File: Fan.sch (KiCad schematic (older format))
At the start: 9 parts

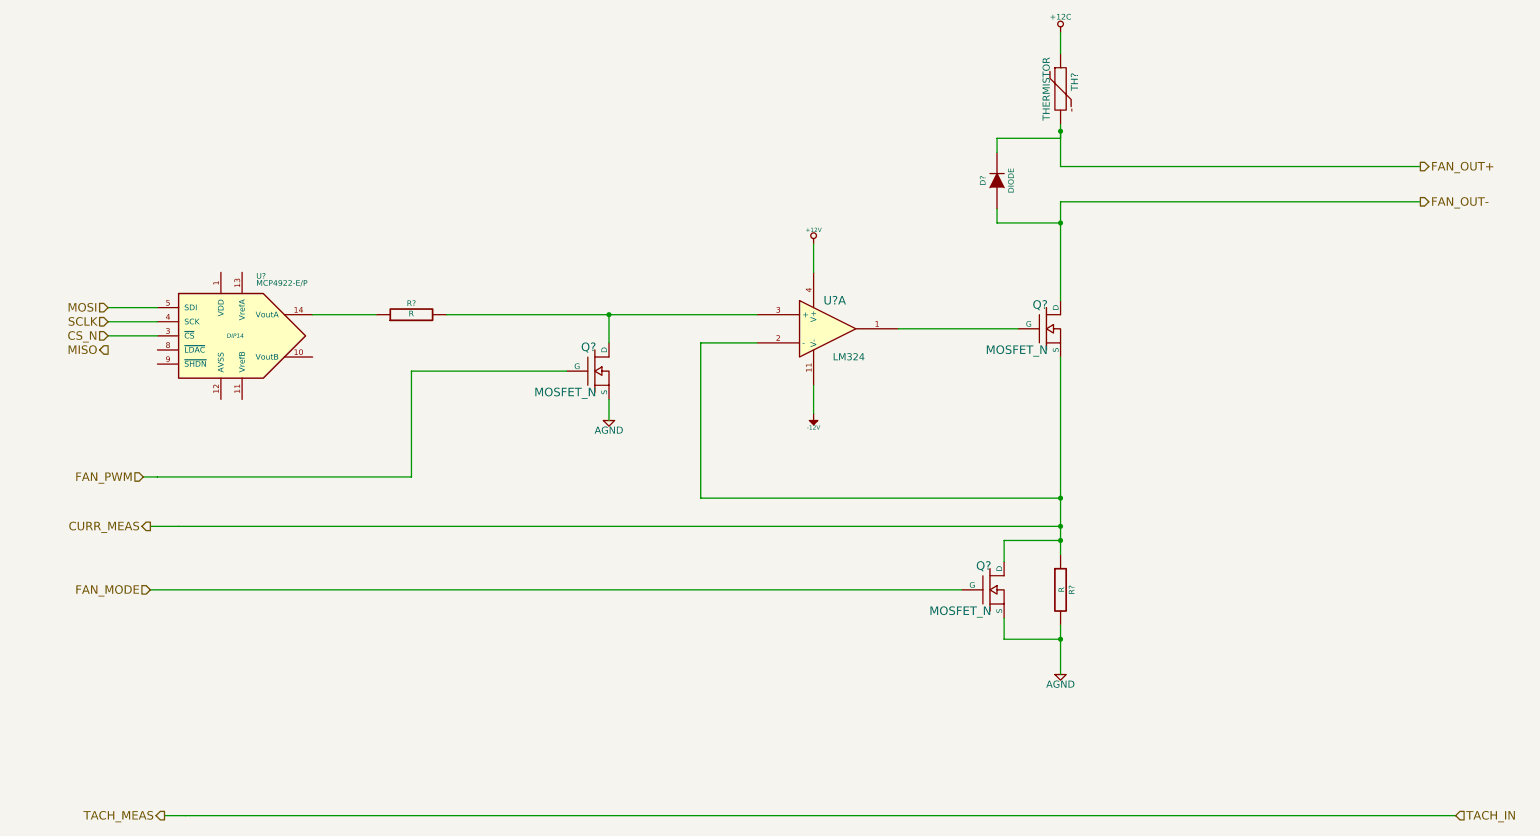
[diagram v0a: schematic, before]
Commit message: Created Footprints and Placed Relay Module
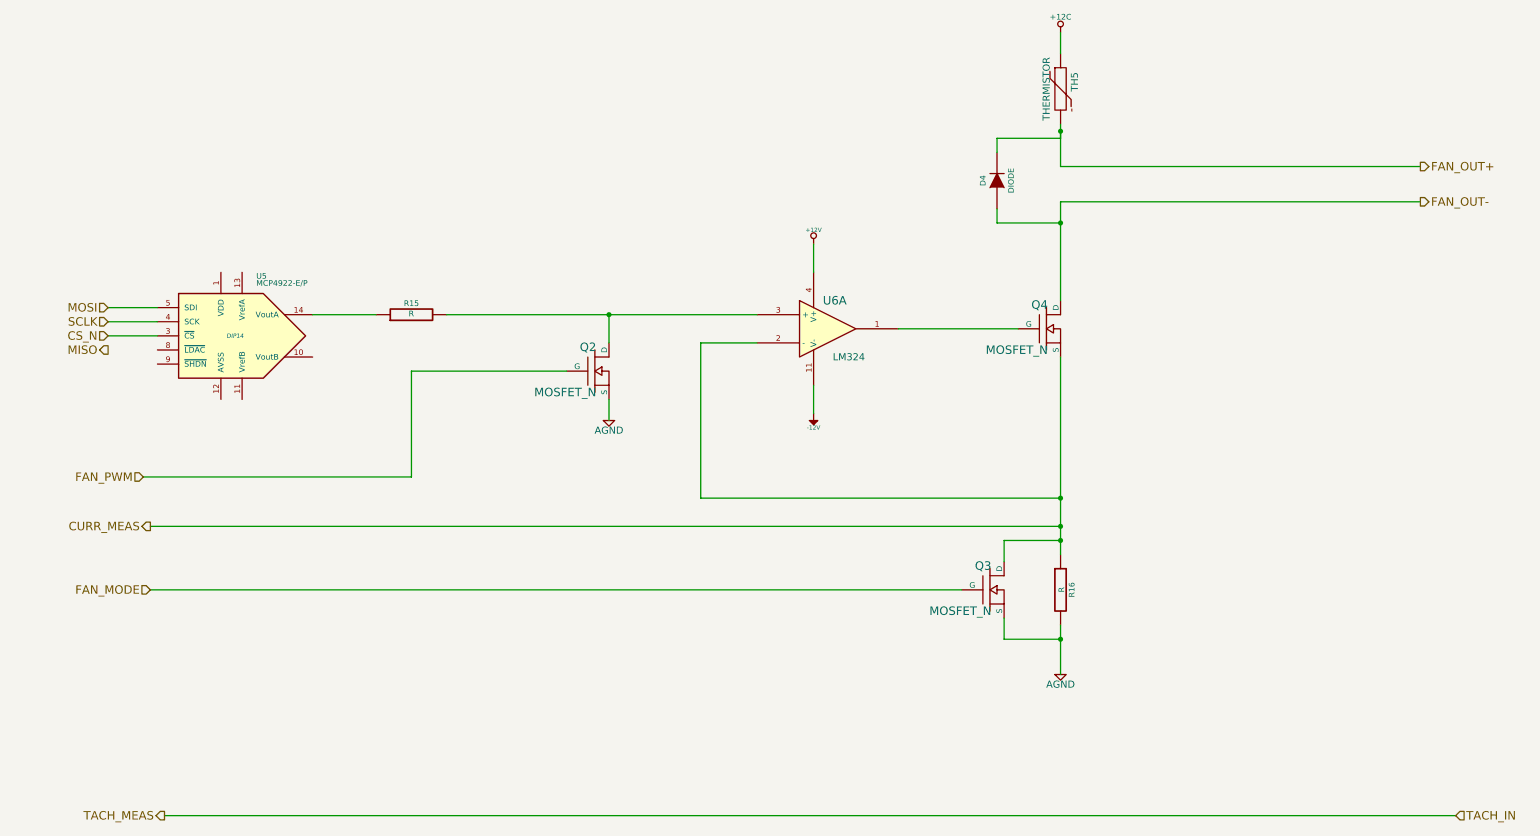
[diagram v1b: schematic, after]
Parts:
- gave numbers to parts that had none: 9
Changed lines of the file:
@@
-EESchema Schematic File Version 2  date 10/10/2013 12:18:22 AM
+EESchema Schematic File Version 2  date 10/10/2013 1:06:29 AM
 LIBS:power
 LIBS:device
@@
 FAN_PWM
 $Comp
-L LM324 U?
+L LM324 U6
 U 1 1 52369784
 P 6250 3100
-F 0 "U?" H 6300 3300 60  0000 C CNN
+F 0 "U6" H 6300 3300 60  0000 C CNN
 F 1 "LM324" H 6400 2900 50  0000 C CNN
 F 2 "" H 6250 3100 60  0000 C CNN
@@
 $EndComp
 $Comp
-L MOSFET_N Q?
+L MOSFET_N Q4
 U 1 1 523697B6
 P 7800 3100
-F 0 "Q?" H 7810 3270 60  0000 R CNN
+F 0 "Q4" H 7810 3270 60  0000 R CNN
 F 1 "MOSFET_N" H 7810 2950 60  0000 R CNN
 F 2 "~" H 7800 3100 60  0000 C CNN
@@
 $EndComp
 $Comp
-L R R?
+L R R16
 U 1 1 523697E7
 P 7900 4950
-F 0 "R?" V 7980 4950 40  0000 C CNN
+F 0 "R16" V 7980 4950 40  0000 C CNN
 F 1 "R" V 7907 4951 40  0000 C CNN
 F 2 "~" V 7830 4950 30  0000 C CNN
@@
 $EndComp
 $Comp
-L AGND #PWR?
+L AGND #PWR31
 U 1 1 523697F6
 P 7900 5550
-F 0 "#PWR?" H 7900 5550 40  0001 C CNN
+F 0 "#PWR31" H 7900 5550 40  0001 C CNN
 F 1 "AGND" H 7900 5480 50  0000 C CNN
 F 2 "" H 7900 5550 60  0000 C CNN
@@
 $EndComp
 $Comp
-L +12V #PWR?
+L +12V #PWR28
 U 1 1 5236981B
 P 6150 2500
-F 0 "#PWR?" H 6150 2450 20  0001 C CNN
+F 0 "#PWR28" H 6150 2450 20  0001 C CNN
 F 1 "+12V" H 6150 2600 30  0000 C CNN
 F 2 "" H 6150 2500 60  0000 C CNN
@@
 $EndComp
 $Comp
-L -12V #PWR?
+L -12V #PWR29
 U 1 1 5236982E
 P 6150 3700
-F 0 "#PWR?" H 6150 3830 20  0001 C CNN
+F 0 "#PWR29" H 6150 3830 20  0001 C CNN
 F 1 "-12V" H 6150 3800 30  0000 C CNN
 F 2 "" H 6150 3700 60  0000 C CNN
@@
 $EndComp
 $Comp
-L AGND #PWR?
+L AGND #PWR27
 U 1 1 523698EE
 P 4700 3750
-F 0 "#PWR?" H 4700 3750 40  0001 C CNN
+F 0 "#PWR27" H 4700 3750 40  0001 C CNN
 F 1 "AGND" H 4700 3680 50  0000 C CNN
 F 2 "" H 4700 3750 60  0000 C CNN
@@
 $EndComp
 $Comp
-L MCP4922-E/P U?
+L MCP4922-E/P U5
 U 1 1 52369914
 P 2050 3150
-F 0 "U?" H 2200 3550 40  0000 L BNN
+F 0 "U5" H 2200 3550 40  0000 L BNN
 F 1 "MCP4922-E/P" H 2200 3500 40  0000 L BNN
 F 2 "DIP14" H 2050 3150 30  0000 C CIN
@@
 CURR_MEAS
 $Comp
-L R R?
+L R R15
 U 1 1 52369992
 P 3300 3000
-F 0 "R?" V 3380 3000 40  0000 C CNN
+F 0 "R15" V 3380 3000 40  0000 C CNN
 F 1 "R" V 3307 3001 40  0000 C CNN
 F 2 "~" V 3230 3000 30  0000 C CNN
@@
 SCLK
 $Comp
-L MOSFET_N Q?
+L MOSFET_N Q3
 U 1 1 5243896F
 P 7400 4950
-F 0 "Q?" H 7410 5120 60  0000 R CNN
+F 0 "Q3" H 7410 5120 60  0000 R CNN
 F 1 "MOSFET_N" H 7410 4800 60  0000 R CNN
 F 2 "~" H 7400 4950 60  0000 C CNN
@@
 $EndComp
 $Comp
-L THERMISTOR TH?
+L THERMISTOR TH5
 U 1 1 5243899F
 P 7900 1400
-F 0 "TH?" V 8000 1450 50  0000 C CNN
+F 0 "TH5" V 8000 1450 50  0000 C CNN
 F 1 "THERMISTOR" V 7800 1400 50  0000 C CNN
 F 2 "~" H 7900 1400 60  0000 C CNN
@@
 $EndComp
 $Comp
-L DIODE D?
+L DIODE D4
 U 1 1 52438A1C
 P 7450 2050
-F 0 "D?" H 7450 2150 40  0000 C CNN
+F 0 "D4" H 7450 2150 40  0000 C CNN
 F 1 "DIODE" H 7450 1950 40  0000 C CNN
 F 2 "~" H 7450 2050 60  0000 C CNN
@@
 $EndComp
 $Comp
-L MOSFET_N Q?
+L MOSFET_N Q2
 U 1 1 52438CB2
 P 4600 3400
-F 0 "Q?" H 4610 3570 60  0000 R CNN
+F 0 "Q2" H 4610 3570 60  0000 R CNN
 F 1 "MOSFET_N" H 4610 3250 60  0000 R CNN
 F 2 "~" H 4600 3400 60  0000 C CNN
@@
 	7600 3100 6750 3100
 Wire Wire Line
-	7900 3300 7900 4300
-Wire Wire Line
-	7900 4300 7900 4500
-Wire Wire Line
-	7900 4500 7900 4600
-Wire Wire Line
-	7900 4600 7900 4700
-Wire Wire Line
-	7900 5200 7900 5300
-Wire Wire Line
-	7900 5300 7900 5550
+	7900 3300 7900 4700
+Wire Wire Line
+	7900 5200 7900 5550
 Wire Wire Line
 	5350 4300 5350 3200
@@
 	6150 3700 6150 3500
 Wire Wire Line
-	3550 3000 4700 3000
-Wire Wire Line
-	4700 3000 5750 3000
+	3550 3000 5750 3000
 Wire Wire Line
 	4700 3600 4700 3750
 Wire Wire Line
-	7900 4500 1650 4500
-Wire Wire Line
-	1650 4500 1450 4500
+	1450 4500 7900 4500
 Connection ~ 7900 4500
 Wire Wire Line
-	1400 4150 1500 4150
-Wire Wire Line
-	1500 4150 3300 4150
+	1400 4150 3300 4150
 Wire Wire Line
 	2600 3000 3050 3000
@@
 	7900 1000 7900 1150
 Wire Wire Line
-	7900 1650 7900 1700
-Wire Wire Line
-	7900 1700 7900 1950
+	7900 1650 7900 1950
 Wire Wire Line
 	7900 1950 10450 1950
@@
 	10450 2200 7900 2200
 Wire Wire Line
-	7900 2200 7900 2350
-Wire Wire Line
-	7900 2350 7900 2900
+	7900 2200 7900 2900
 Wire Wire Line
 	7900 2350 7450 2350
@@
 Connection ~ 7900 5300
 Wire Wire Line
-	1700 6550 10700 6550
-Wire Wire Line
-	1700 6550 1550 6550
+	1550 6550 10700 6550
 Wire Wire Line
 	4400 3400 3300 3400
@@
 FAN_MODE
 $Comp
-L +12C #PWR?
+L +12C #PWR30
 U 1 1 5243907A
 P 7900 1000
-F 0 "#PWR?" H 7900 970 30  0001 C CNN
+F 0 "#PWR30" H 7900 970 30  0001 C CNN
 F 1 "+12C" H 7900 1110 40  0000 C CNN
 F 2 "~" H 7900 1000 60  0000 C CNN

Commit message: Associating Thermocouple Module Components
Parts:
- U4: renamed from U6; value LM324 -> OPA4170
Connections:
- net CURR_MEAS: now also U4.6 (-); no longer U4.2 (-)
- net at Q4.1 (G): now also U4.7; no longer U4.1
- net at Q2.2 (D), R15.2: now also U4.5 (+); no longer U4.3 (+)
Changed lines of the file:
@@
-EESchema Schematic File Version 2  date 10/10/2013 1:06:29 AM
+EESchema Schematic File Version 2  date 10/11/2013 1:04:35 AM
 LIBS:power
 LIBS:device
@@
 $Descr A4 11693 8268
 encoding utf-8
-Sheet 4 9
+Sheet 9 9
 Title ""
-Date "10 oct 2013"
+Date "11 oct 2013"
 Rev ""
 Comp ""
@@
 FAN_PWM
 $Comp
-L LM324 U6
-U 1 1 52369784
+L LM324 U4
+U 2 1 52369784
 P 6250 3100
-F 0 "U6" H 6300 3300 60  0000 C CNN
-F 1 "LM324" H 6400 2900 50  0000 C CNN
+F 0 "U4" H 6300 3300 60  0000 C CNN
+F 1 "OPA4170" H 6400 2900 50  0000 C CNN
 F 2 "" H 6250 3100 60  0000 C CNN
 F 3 "" H 6250 3100 60  0000 C CNN
-	1    6250 3100
+	2    6250 3100
 	1    0    0    -1
 $EndComp
@@
 $EndComp
 $Comp
-L AGND #PWR31
+L AGND #PWR053
 U 1 1 523697F6
 P 7900 5550
-F 0 "#PWR31" H 7900 5550 40  0001 C CNN
+F 0 "#PWR053" H 7900 5550 40  0001 C CNN
 F 1 "AGND" H 7900 5480 50  0000 C CNN
 F 2 "" H 7900 5550 60  0000 C CNN
@@
 $EndComp
 $Comp
-L +12V #PWR28
+L +12V #PWR054
 U 1 1 5236981B
 P 6150 2500
-F 0 "#PWR28" H 6150 2450 20  0001 C CNN
+F 0 "#PWR054" H 6150 2450 20  0001 C CNN
 F 1 "+12V" H 6150 2600 30  0000 C CNN
 F 2 "" H 6150 2500 60  0000 C CNN
@@
 $EndComp
 $Comp
-L -12V #PWR29
+L -12V #PWR055
 U 1 1 5236982E
 P 6150 3700
-F 0 "#PWR29" H 6150 3830 20  0001 C CNN
+F 0 "#PWR055" H 6150 3830 20  0001 C CNN
 F 1 "-12V" H 6150 3800 30  0000 C CNN
 F 2 "" H 6150 3700 60  0000 C CNN
@@
 $EndComp
 $Comp
-L AGND #PWR27
+L AGND #PWR056
 U 1 1 523698EE
 P 4700 3750
-F 0 "#PWR27" H 4700 3750 40  0001 C CNN
+F 0 "#PWR056" H 4700 3750 40  0001 C CNN
 F 1 "AGND" H 4700 3680 50  0000 C CNN
 F 2 "" H 4700 3750 60  0000 C CNN
@@
 FAN_MODE
 $Comp
-L +12C #PWR30
+L +12C #PWR057
 U 1 1 5243907A
 P 7900 1000
-F 0 "#PWR30" H 7900 970 30  0001 C CNN
+F 0 "#PWR057" H 7900 970 30  0001 C CNN
 F 1 "+12C" H 7900 1110 40  0000 C CNN
 F 2 "~" H 7900 1000 60  0000 C CNN
